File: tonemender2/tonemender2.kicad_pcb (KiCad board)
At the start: 2 copper layers, 90.8 x 54.1 mm, 41 parts, among them J1 JACK_STEREO, J2 Conn_01x02, J3 Conn_01x02, J4 JACK_STEREO, J5 Conn_01x02, P1 CONN_01X01, P2 CONN_01X01, SW1 SW_DPST_x2, SW2 SW_DPST_x2, U1 OPA1612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

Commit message: Update copyright on tonemender2
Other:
- board text added: "(C) 2014-2022 Jon Ronen-Drori github.com/jonronen"
- board text removed: "(C) 2014-2016 Jon Ronen-Drori github.com/jonronen"
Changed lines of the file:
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@@
     (effects (font (size 1.5 1.5) (thickness 0.3)))
   )
-  (gr_text "(C) 2014-2016\nJon Ronen-Drori\ngithub.com/jonronen" (at 205.74 109.855) (layer B.SilkS)
+  (gr_text "(C) 2014-2022\nJon Ronen-Drori\ngithub.com/jonronen" (at 205.74 109.855) (layer B.SilkS)
     (effects (font (size 1.5 1.5) (thickness 0.3)) (justify left mirror))
   )

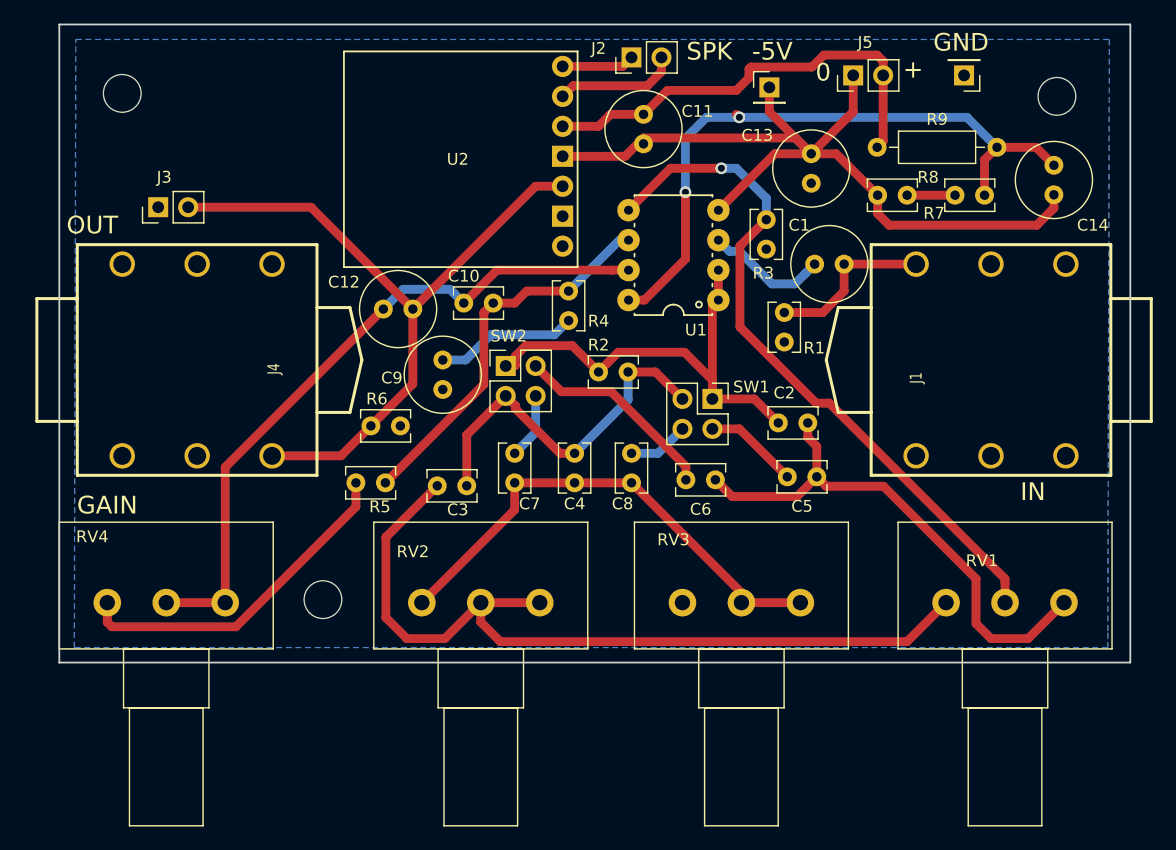
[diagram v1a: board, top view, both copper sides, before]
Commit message: Fix edge cuts on tonemender2
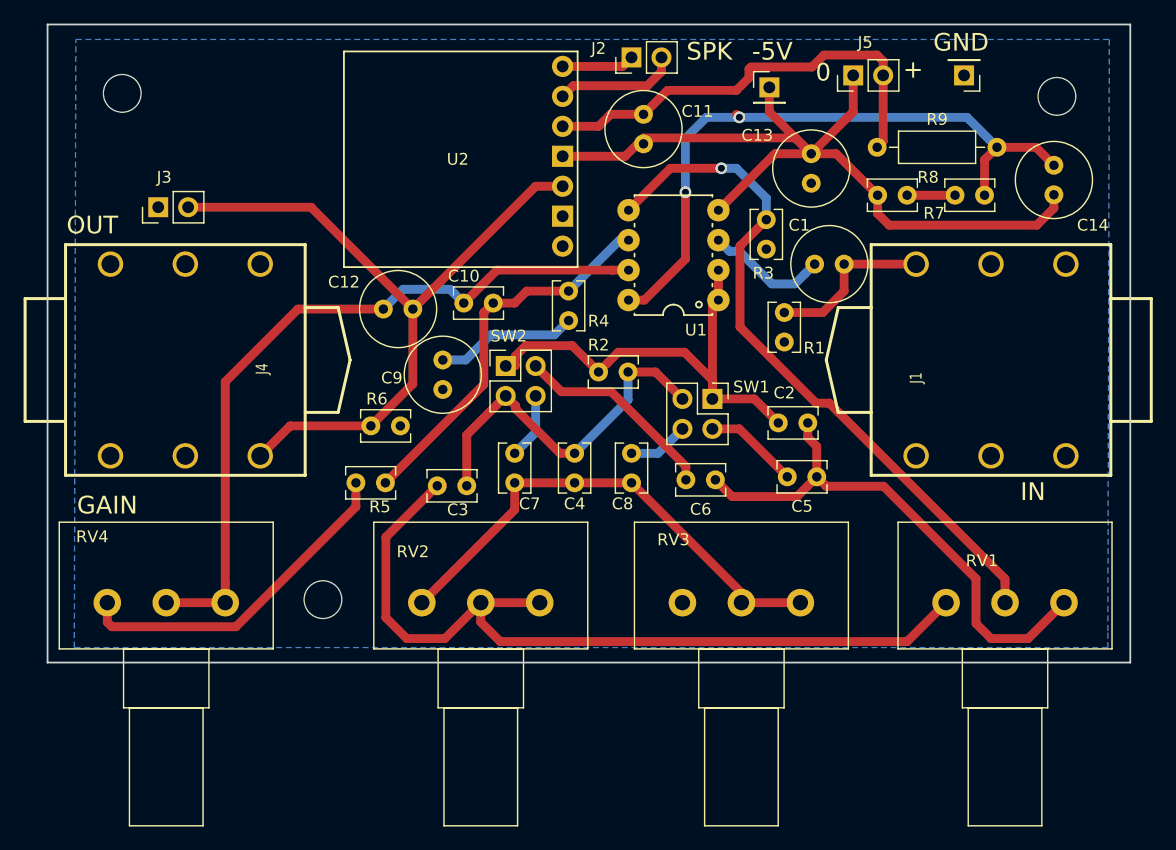
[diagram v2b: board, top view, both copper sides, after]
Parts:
- moved J4 1.00 mm to (128.8, 106.8)
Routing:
- net Net-(C10-Pad1): track 58.6 -> 62.8 mm
- net /PreAmpOut: track 60.5 -> 61.5 mm
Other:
- board size 90.8 x 54.1 mm -> 91.8 x 54.1 mm
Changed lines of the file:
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@@
     (thickness 1.6)
     (drawings 13)
-    (tracks 182)
+    (tracks 184)
     (zones 0)
     (modules 41)
@@
     (add_net "Net-(R5-Pad1)")
   )
+  (module my_shit:audio_635mm_stereo_input (layer F.Cu)
+    (at 128.794 106.807)
+    (descr "stereo audio 6.35mm input")
+    (fp_text reference J4 (at 6.5024 1.016 90) (layer F.SilkS)
+      (effects (font (size 1.016 0.762) (thickness 0.127)))
+    )
+    (fp_text value JACK_STEREO (at 6.5024 2.3368 90) (layer F.SilkS) hide
+      (effects (font (size 1.016 0.762) (thickness 0.127)))
+    )
+    (fp_line (start -10.16 -9.525) (end -10.16 10.033) (layer F.SilkS) (width 0.254))
+    (fp_line (start -10.16 -4.953) (end -13.589 -4.953) (layer F.SilkS) (width 0.254))
+    (fp_line (start -13.589 -4.953) (end -13.589 5.461) (layer F.SilkS) (width 0.254))
+    (fp_line (start -13.589 5.461) (end -10.16 5.461) (layer F.SilkS) (width 0.254))
+    (fp_line (start -10.16 10.033) (end 10.16 10.033) (layer F.SilkS) (width 0.254))
+    (fp_line (start 10.16 10.033) (end 10.16 -9.525) (layer F.SilkS) (width 0.254))
+    (fp_line (start 10.16 4.699) (end 12.954 4.699) (layer F.SilkS) (width 0.254))
+    (fp_line (start 12.954 4.699) (end 13.97 0.254) (layer F.SilkS) (width 0.254))
+    (fp_line (start 13.97 0.254) (end 12.954 -4.191) (layer F.SilkS) (width 0.254))
+    (fp_line (start 12.954 -4.191) (end 10.16 -4.191) (layer F.SilkS) (width 0.254))
+    (fp_line (start 10.16 -9.525) (end -10.16 -9.525) (layer F.SilkS) (width 0.254))
+    (pad 1 thru_hole circle (at -6.35 8.382) (size 2.159 2.159) (drill 1.524) (layers *.Cu *.Mask F.SilkS)
+      (net 8 GND))
+    (pad 2 thru_hole circle (at 6.35 8.382) (size 2.159 2.159) (drill 1.524) (layers *.Cu *.Mask F.SilkS)
+      (net 20 /PreAmpOut))
+    (pad 3 thru_hole circle (at 0 8.382) (size 2.159 2.159) (drill 1.524) (layers *.Cu *.Mask F.SilkS))
+    (pad 4 thru_hole circle (at -6.35 -7.874) (size 2.159 2.159) (drill 1.524) (layers *.Cu *.Mask F.SilkS)
+      (net 8 GND))
+    (pad 5 thru_hole circle (at 6.35 -7.874) (size 2.159 2.159) (drill 1.524) (layers *.Cu *.Mask F.SilkS)
+      (net 8 GND))
+    (pad 6 thru_hole circle (at 0 -7.874) (size 2.159 2.159) (drill 1.524) (layers *.Cu *.Mask F.SilkS))
+  )
   (module Capacitor_THT:C_Radial_D6.3mm_H5.0mm_P2.50mm (layer F.Cu)
     (at 150.622 107.061 270)
@@
     (pad 7 thru_hole circle (at 9.398 7.366) (size 1.8 1.8) (drill 1) (layers *.Cu *.Mask F.SilkS))
   )
-  (module my_shit:audio_635mm_stereo_input (layer F.Cu)
-    (at 129.794 106.807)
-    (descr "stereo audio 6.35mm input")
-    (fp_text reference J4 (at 6.5024 1.016 90) (layer F.SilkS)
-      (effects (font (size 1.016 0.762) (thickness 0.127)))
-    )
-    (fp_text value JACK_STEREO (at 6.5024 2.3368 90) (layer F.SilkS) hide
-      (effects (font (size 1.016 0.762) (thickness 0.127)))
-    )
-    (fp_line (start -10.16 -9.525) (end -10.16 10.033) (layer F.SilkS) (width 0.254))
-    (fp_line (start -10.16 -4.953) (end -13.589 -4.953) (layer F.SilkS) (width 0.254))
-    (fp_line (start -13.589 -4.953) (end -13.589 5.461) (layer F.SilkS) (width 0.254))
-    (fp_line (start -13.589 5.461) (end -10.16 5.461) (layer F.SilkS) (width 0.254))
-    (fp_line (start -10.16 10.033) (end 10.16 10.033) (layer F.SilkS) (width 0.254))
-    (fp_line (start 10.16 10.033) (end 10.16 -9.525) (layer F.SilkS) (width 0.254))
-    (fp_line (start 10.16 4.699) (end 12.954 4.699) (layer F.SilkS) (width 0.254))
-    (fp_line (start 12.954 4.699) (end 13.97 0.254) (layer F.SilkS) (width 0.254))
-    (fp_line (start 13.97 0.254) (end 12.954 -4.191) (layer F.SilkS) (width 0.254))
-    (fp_line (start 12.954 -4.191) (end 10.16 -4.191) (layer F.SilkS) (width 0.254))
-    (fp_line (start 10.16 -9.525) (end -10.16 -9.525) (layer F.SilkS) (width 0.254))
-    (pad 1 thru_hole circle (at -6.35 8.382) (size 2.159 2.159) (drill 1.524) (layers *.Cu *.Mask F.SilkS)
-      (net 8 GND))
-    (pad 2 thru_hole circle (at 6.35 8.382) (size 2.159 2.159) (drill 1.524) (layers *.Cu *.Mask F.SilkS)
-      (net 20 /PreAmpOut))
-    (pad 3 thru_hole circle (at 0 8.382) (size 2.159 2.159) (drill 1.524) (layers *.Cu *.Mask F.SilkS))
-    (pad 4 thru_hole circle (at -6.35 -7.874) (size 2.159 2.159) (drill 1.524) (layers *.Cu *.Mask F.SilkS)
-      (net 8 GND))
-    (pad 5 thru_hole circle (at 6.35 -7.874) (size 2.159 2.159) (drill 1.524) (layers *.Cu *.Mask F.SilkS)
-      (net 8 GND))
-    (pad 6 thru_hole circle (at 0 -7.874) (size 2.159 2.159) (drill 1.524) (layers *.Cu *.Mask F.SilkS))
-  )
   (module Capacitor_THT:C_Radial_D6.3mm_H5.0mm_P2.50mm (layer F.Cu)
     (at 182.15 98.933)
@@
     (effects (font (size 1.5 1.5) (thickness 0.3)))
   )
-  (gr_text "(C) 2014-2022\nJon Ronen-Drori\ngithub.com/jonronen" (at 205.74 109.855) (layer B.SilkS)
+  (gr_text "(C) 2014-2022\nJon Ronen-Drori\ngithub.com/jonronen" (at 206.502 105.537) (layer B.SilkS)
     (effects (font (size 1.5 1.5) (thickness 0.3)) (justify left mirror))
   )
@@
     (effects (font (size 1.5 1.5) (thickness 0.3)))
   )
-  (gr_line (start 118.11 132.715) (end 118.11 78.613) (angle 90) (layer Edge.Cuts) (width 0.15))
+  (gr_line (start 117.11 132.715) (end 117.11 78.613) (angle 90) (layer Edge.Cuts) (width 0.15))
   (gr_line (start 208.915 78.613) (end 208.915 132.715) (angle 90) (layer Edge.Cuts) (width 0.15))
   (gr_text GAIN (at 122.174 119.38) (layer F.SilkS)
@@
     (effects (font (size 1.5 1.5) (thickness 0.25)))
   )
-  (gr_line (start 118.11 78.613) (end 208.915 78.613) (angle 90) (layer Edge.Cuts) (width 0.15))
-  (gr_line (start 208.915 132.715) (end 118.11 132.715) (angle 90) (layer Edge.Cuts) (width 0.15))
+  (gr_line (start 117.11 78.613) (end 208.915 78.613) (angle 90) (layer Edge.Cuts) (width 0.15))
+  (gr_line (start 208.915 132.715) (end 117.11 132.715) (angle 90) (layer Edge.Cuts) (width 0.15))
   (segment (start 178.519999 100.608001) (end 180.474999 100.608001) (width 0.75) (layer B.Cu) (net 1))
   (segment (start 181.350001 99.732999) (end 182.15 98.933) (width 0.75) (layer B.Cu) (net 1))
@@
   (segment (start 147.257001 101.067999) (end 151.232999 101.067999) (width 0.75) (layer B.Cu) (net 17))
   (segment (start 145.582 102.743) (end 147.257001 101.067999) (width 0.75) (layer B.Cu) (net 17))
-  (segment (start 132.174 116.151) (end 132.174 127.635) (width 0.75) (layer F.Cu) (net 17))
-  (segment (start 145.582 102.743) (end 132.174 116.151) (width 0.75) (layer F.Cu) (net 17))
+  (segment (start 132.174 108.916338) (end 132.174 125.980371) (width 0.75) (layer F.Cu) (net 17))
+  (segment (start 132.174 125.980371) (end 132.174 127.635) (width 0.75) (layer F.Cu) (net 17))
+  (segment (start 138.347338 102.743) (end 132.174 108.916338) (width 0.75) (layer F.Cu) (net 17))
+  (segment (start 145.582 102.743) (end 138.347338 102.743) (width 0.75) (layer F.Cu) (net 17))
   (segment (start 178.308 86.019) (end 181.864 89.575) (width 0.75) (layer F.Cu) (net 18) (status 20))
   (segment (start 178.308 83.947) (end 178.308 86.019) (width 0.75) (layer F.Cu) (net 18) (status 10))
@@
   (segment (start 171.196 88.265) (end 172.974 86.487) (width 0.75) (layer B.Cu) (net 19))
   (segment (start 171.196 92.837) (end 171.196 88.265) (width 0.75) (layer B.Cu) (net 19))
-  (segment (start 141.986 115.189) (end 144.526 112.649) (width 0.75) (layer F.Cu) (net 20))
-  (segment (start 136.144 115.189) (end 141.986 115.189) (width 0.75) (layer F.Cu) (net 20))
   (segment (start 148.082 109.093) (end 144.526 112.649) (width 0.75) (layer F.Cu) (net 20))
   (segment (start 148.082 102.743) (end 148.082 109.093) (width 0.75) (layer F.Cu) (net 20))
@@
   (segment (start 139.446 94.107) (end 148.082 102.743) (width 0.75) (layer F.Cu) (net 20))
   (segment (start 129.032 94.107) (end 139.446 94.107) (width 0.75) (layer F.Cu) (net 20))
+  (segment (start 137.684 112.649) (end 144.526 112.649) (width 0.75) (layer F.Cu) (net 20))
+  (segment (start 135.144 115.189) (end 137.684 112.649) (width 0.75) (layer F.Cu) (net 20))
   (segment (start 169.164 82.609081) (end 169.164 81.407) (width 0.75) (layer F.Cu) (net 21) (status 20))
   (segment (start 167.96408 83.809001) (end 169.164 82.609081) (width 0.75) (layer F.Cu) (net 21))
